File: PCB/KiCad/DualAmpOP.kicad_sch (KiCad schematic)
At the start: 8 parts, among them J1 Conn_01x06_Pin, P1 value, U1 MCP6002

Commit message: Nouvelle version 2 plus pratique
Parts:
- removed J1: Conn_01x06_Pin, symbol Connector:Conn_01x06_Pin
- removed P1: value, 00_Resistor:Potentiometer_Bourns_3296W_Vertical, symbol 00_Resistor:Trimmer_Potentiometer_model
- removed unit 2 of U1
- added C1, C2: value, 00_Capacitor:C_0805_2012Metric_Pad1.18x1.45mm_HandSolder, symbol 00_Capacitor:C_0805
- added J1: (no value), Connector_PinHeader_2.54mm:PinHeader_1x06_P2.54mm_Vertical, symbol 00_Connector:Pin_01x06
- added J2: (no value), Connector_PinHeader_2.54mm:PinHeader_1x04_P2.54mm_Vertical, symbol 00_Connector:Pin_01x04
- added R10, R14, R17, R6, R7, R8, R9: value, Resistor_SMD:R_0805_2012Metric_Pad1.20x1.40mm_HandSolder, symbol 00_Resistor:R_0805
- added R11, R12, R13, R15: R, Resistor_SMD:R_0805_2012Metric_Pad1.20x1.40mm_HandSolder, symbol Device:R
- added unit 2 of U1
- R1: renamed from R2; footprint (none) -> Resistor_SMD:R_0805_2012Metric_Pad1.20x1.40mm_HandSolder
- R2: renamed from R4; footprint (none) -> Resistor_SMD:R_0805_2012Metric_Pad1.20x1.40mm_HandSolder
- R3, R5: footprint (none) -> Resistor_SMD:R_0805_2012Metric_Pad1.20x1.40mm_HandSolder
- R4: renamed from R1; footprint 00_Resistor:R_0805_2012Metric_Pad1.20x1.40mm_HandSolder -> Resistor_SMD:R_0805_2012Metric_Pad1.20x1.40mm_HandSolder
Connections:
- net GND: now also R5.1, C1.2, C2.2, J1.5 (Pin_5), J2.4 (Pin_4), R10.2, R15.1, R17.1, R7.1; no longer R3.2, R5.2
- net at R1.1: now also J1.3 (Pin_3); no longer R5.1
- net at R1.2, U1.2 (-): now also R3.1, R7.2; no longer R2.1
- net at U1.1: now also R3.2, R4.2, J1.4 (Pin_4), R9.1; no longer R2.2
- net at R4.1: now also R2.2, R5.2, U1.3 (+), R6.2
- net at U1.4 (V-): now also C2.1, J1.6 (Pin_6), R10.1
- net at U1.8 (V+): now also C1.1, J1.1 (Pin_1)
- new net: J2.1 (Pin_1), R12.2, R14.1, R15.2, U1.5 (+)
- new net: J2.2 (Pin_2), R11.2, R13.1, R17.2, U1.6 (-)
- new net: J2.3 (Pin_3), R13.2, R14.2, U1.7
- new net: R11.1, R12.1, R9.2
- new net: R2.1, R6.1, R8.2
- new net: J1.2 (Pin_2), R8.1
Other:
- moved on the sheet: R1, R2, R3, R4, R5, U1A, U1C

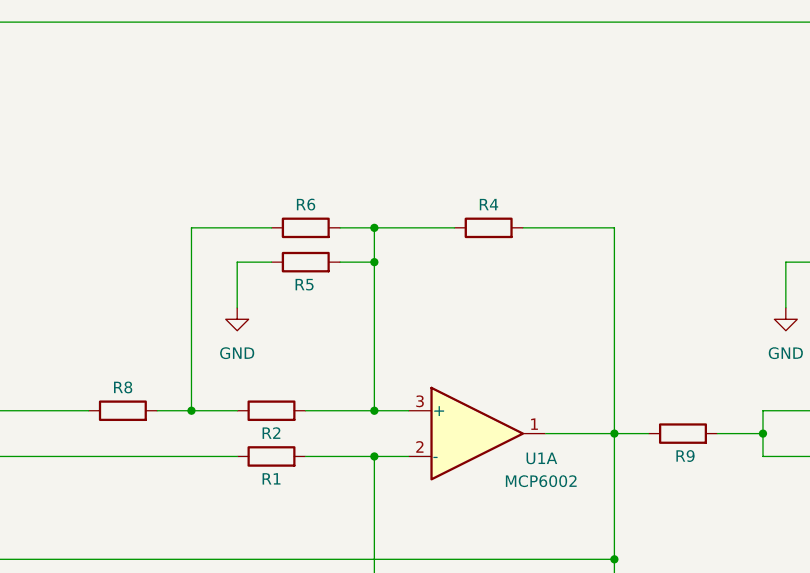
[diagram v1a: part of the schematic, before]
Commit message: Modification R6 pour filtre Sallen-key
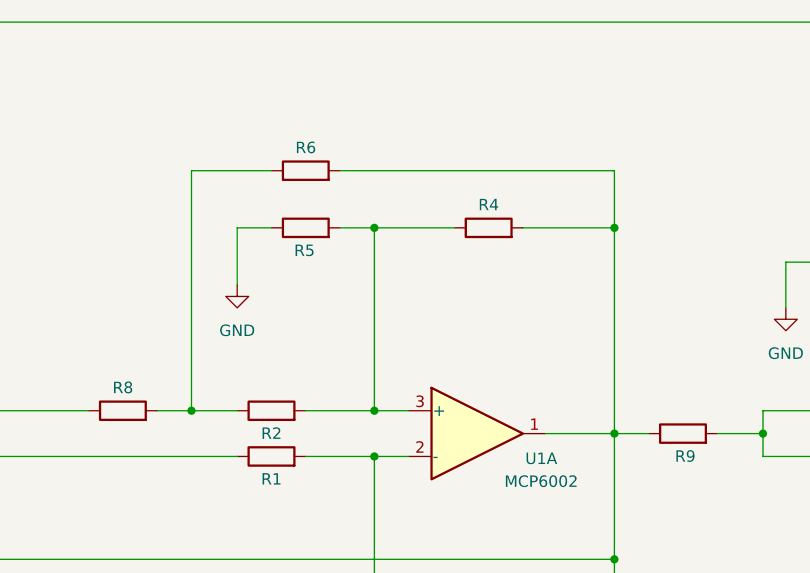
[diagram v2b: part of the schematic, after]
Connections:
- net at J1.4 (Pin_4), R3.2, R4.2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: now also R6.2
- net at R2.2, R4.1, R5.2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: no longer R6.2
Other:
- moved on the sheet: R5, R6
